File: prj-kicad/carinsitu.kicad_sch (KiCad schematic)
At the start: 57 parts, among them P1 BAT, P2 MOT, P3 CONN_3, P4 CONN_1, P5 CONN_4, SW1 SWITCH_SLIDE, U1 ESP8285, U2 MIC2860, U3 MAX17205, U4 SN74LVC1T45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

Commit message: Fix schematic DRC
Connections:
- no-connect marks 7 -> 15
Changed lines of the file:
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@@
   (junction (at 40.64 181.61) (diameter 0) (color 0 0 0 0)
   )
+  (junction (at 71.12 128.27) (diameter 0) (color 0 0 0 0)
+  )
   (junction (at 50.8 73.66) (diameter 0) (color 0 0 0 0)
   )
@@
   )
   (no_connect (at 210.82 96.52))
+  (no_connect (at 78.74 40.64))
+  (no_connect (at 78.74 35.56))
   (no_connect (at 210.82 101.6))
+  (no_connect (at 82.55 175.26))
   (no_connect (at 125.73 31.75))
+  (no_connect (at 78.74 43.18))
   (no_connect (at 111.76 48.26))
+  (no_connect (at 78.74 38.1))
   (no_connect (at 82.55 165.1))
+  (no_connect (at 78.74 45.72))
+  (no_connect (at 111.76 45.72))
   (no_connect (at 259.08 109.22))
   (no_connect (at 66.04 133.35))
+  (no_connect (at 78.74 48.26))
   (wire (pts (xy 242.57 148.59) (xy 242.57 137.16))
     (stroke (width 0) (type default) (color 0 0 0 0))
@@
     (stroke (width 0) (type default) (color 0 0 0 0))
   )
+  (wire (pts (xy 71.12 128.27) (xy 72.39 128.27))
+    (stroke (width 0) (type default) (color 0 0 0 0))
+  )
   (wire (pts (xy 128.27 78.74) (xy 128.27 77.47))
     (stroke (width 0) (type default) (color 0 0 0 0))
@@
     (pin "2")
   )
+  (symbol (lib_id "power:PWR_FLAG") (at 72.39 128.27 270) (unit 1)
+    (in_bom yes) (on_board yes) (fields_autoplaced)
+    (property "Reference" "#FLG0101" (id 0) (at 74.295 128.27 0)
+      (effects (font (size 1.27 1.27)) hide)
+    )
+    (property "Value" "PWR_FLAG" (id 1) (at 75.565 128.7038 90)
+      (effects (font (size 1.27 1.27)) (justify left))
+    )
+    (property "Footprint" "" (id 2) (at 72.39 128.27 0)
+      (effects (font (size 1.27 1.27)) hide)
+    )
+    (property "Datasheet" "~" (id 3) (at 72.39 128.27 0)
+      (effects (font (size 1.27 1.27)) hide)
+    )
+    (pin "1")
+  )
   (sheet (at 102.87 120.65) (size 67.31 41.91) (fields_autoplaced)
     (stroke (width 0) (type solid) (color 0 0 0 0))
@@
   )
   (symbol_instances
+    (path "/72432868-7bcd-4a68-adb7-1800ac178c45"
+      (reference "#FLG0101") (unit 1) (value "PWR_FLAG") (footprint "")
+    )
+    (path "/00000000-0000-0000-0000-00005d24ff79/10e431fa-02a9-4f70-8adb-f2c11e9e1180"
+      (reference "#FLG0102") (unit 1) (value "PWR_FLAG") (footprint "")
+    )
+    (path "/00000000-0000-0000-0000-00005d24ff79/f57f5fed-3b45-4cb3-9d9d-82cd0401c166"
+      (reference "#FLG0103") (unit 1) (value "PWR_FLAG") (footprint "")
+    )
     (path "/00000000-0000-0000-0000-00005d08ea24"
       (reference "#PWR01") (unit 1) (value "GND") (footprint "")

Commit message: Do TODO for rear lights
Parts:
- removed D3: LED_APA106, carinsitu:LED-APA106, symbol carinsitu:LED_APA106
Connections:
- net at D4.4 (DIN): now also U4.4 (B)
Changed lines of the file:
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@@
     (stroke (width 0) (type default) (color 0 0 0 0))
   )
+  (wire (pts (xy 254 99.06) (xy 254 106.68))
+    (stroke (width 0) (type default) (color 0 0 0 0))
+  )
   (wire (pts (xy 199.39 111.76) (xy 199.39 113.03))
     (stroke (width 0) (type default) (color 0 0 0 0))
@@
     (stroke (width 0) (type default) (color 0 0 0 0))
   )
-  (wire (pts (xy 250.19 87.63) (xy 250.19 99.06))
-    (stroke (width 0) (type default) (color 0 0 0 0))
-  )
   (wire (pts (xy 71.12 128.27) (xy 66.04 128.27))
     (stroke (width 0) (type default) (color 0 0 0 0))
@@
     (stroke (width 0) (type default) (color 0 0 0 0))
   )
-  (wire (pts (xy 250.19 87.63) (xy 259.08 87.63))
-    (stroke (width 0) (type default) (color 0 0 0 0))
-  )
   (wire (pts (xy 109.22 43.18) (xy 109.22 40.64))
     (stroke (width 0) (type default) (color 0 0 0 0))
@@
     (stroke (width 0) (type default) (color 0 0 0 0))
   )
-  (wire (pts (xy 256.54 92.71) (xy 259.08 92.71))
-    (stroke (width 0) (type default) (color 0 0 0 0))
-  )
   (wire (pts (xy 193.04 86.36) (xy 193.04 87.63))
     (stroke (width 0) (type default) (color 0 0 0 0))
@@
     (stroke (width 0) (type default) (color 0 0 0 0))
   )
-  (wire (pts (xy 250.19 99.06) (xy 246.38 99.06))
+  (wire (pts (xy 246.38 99.06) (xy 254 99.06))
     (stroke (width 0) (type default) (color 0 0 0 0))
   )
@@
     (stroke (width 0) (type default) (color 0 0 0 0))
   )
-  (wire (pts (xy 256.54 82.55) (xy 256.54 85.09))
-    (stroke (width 0) (type default) (color 0 0 0 0))
-  )
   (wire (pts (xy 227.33 137.16) (xy 228.6 137.16))
     (stroke (width 0) (type default) (color 0 0 0 0))
@@
     (stroke (width 0) (type default) (color 0 0 0 0))
   )
-  (wire (pts (xy 256.54 95.25) (xy 256.54 92.71))
-    (stroke (width 0) (type default) (color 0 0 0 0))
-  )
   (wire (pts (xy 196.85 110.49) (xy 196.85 111.76))
     (stroke (width 0) (type default) (color 0 0 0 0))
@@
     (stroke (width 0) (type default) (color 0 0 0 0))
   )
-  (wire (pts (xy 259.08 90.17) (xy 254 90.17))
-    (stroke (width 0) (type default) (color 0 0 0 0))
-  )
   (wire (pts (xy 242.57 137.16) (xy 246.38 137.16))
     (stroke (width 0) (type default) (color 0 0 0 0))
@@
     (stroke (width 0) (type default) (color 0 0 0 0))
   )
-  (wire (pts (xy 256.54 85.09) (xy 259.08 85.09))
-    (stroke (width 0) (type default) (color 0 0 0 0))
-  )
   (wire (pts (xy 43.18 50.8) (xy 45.72 50.8))
     (stroke (width 0) (type default) (color 0 0 0 0))
@@
     (stroke (width 0) (type default) (color 0 0 0 0))
   )
-  (wire (pts (xy 254 90.17) (xy 254 106.68))
-    (stroke (width 0) (type default) (color 0 0 0 0))
-  )
   (wire (pts (xy 43.18 44.45) (xy 45.72 44.45))
     (stroke (width 0) (type default) (color 0 0 0 0))
@@
     (pin "1")
   )
-  (symbol (lib_id "carinsitu:LED_APA106") (at 266.7 88.9 0) (unit 1)
-    (in_bom yes) (on_board yes)
-    (property "Reference" "D3" (id 0) (at 266.7 82.55 0)
-      (effects (font (size 1.524 1.524)))
-    )
-    (property "Value" "LED_APA106" (id 1) (at 266.7 88.9 90)
-      (effects (font (size 1.016 1.016)))
-    )
-    (property "Footprint" "carinsitu:LED-APA106" (id 2) (at 266.7 88.9 0)
-      (effects (font (size 1.524 1.524)) hide)
-    )
-    (property "Datasheet" "" (id 3) (at 266.7 88.9 0)
-      (effects (font (size 1.524 1.524)))
-    )
-    (pin "1")
-    (pin "2")
-    (pin "3")
-    (pin "4")
-  )
   (symbol (lib_id "carinsitu:LED_APA106") (at 266.7 107.95 0) (unit 1)
     (in_bom yes) (on_board yes)
@@
     (pin "4")
   )
-  (symbol (lib_id "carinsitu:+5V") (at 256.54 82.55 0) (unit 1)
-    (in_bom yes) (on_board yes)
-    (property "Reference" "#PWR027" (id 0) (at 256.54 83.566 0)
-      (effects (font (size 0.762 0.762)) hide)
-    )
-    (property "Value" "+5V" (id 1) (at 256.54 79.756 0)
-      (effects (font (size 0.762 0.762)))
-    )
-    (property "Footprint" "" (id 2) (at 256.54 82.55 0)
-      (effects (font (size 1.524 1.524)))
-    )
-    (property "Datasheet" "" (id 3) (at 256.54 82.55 0)
-      (effects (font (size 1.524 1.524)))
-    )
-    (pin "1")
-  )
-  (symbol (lib_id "carinsitu:GND") (at 256.54 95.25 0) (unit 1)
-    (in_bom yes) (on_board yes)
-    (property "Reference" "#PWR028" (id 0) (at 256.54 95.25 0)
-      (effects (font (size 0.762 0.762)) hide)
-    )
-    (property "Value" "GND" (id 1) (at 256.54 97.028 0)
-      (effects (font (size 0.762 0.762)) hide)
-    )
-    (property "Footprint" "" (id 2) (at 256.54 95.25 0)
-      (effects (font (size 1.524 1.524)))
-    )
-    (property "Datasheet" "" (id 3) (at 256.54 95.25 0)
-      (effects (font (size 1.524 1.524)))
-    )
-    (pin "1")
-  )
   (symbol (lib_id "carinsitu:+5V") (at 256.54 101.6 0) (unit 1)
     (in_bom yes) (on_board yes)
@@
       (reference "#PWR026") (unit 1) (value "GND") (footprint "")
     )
-    (path "/00000000-0000-0000-0000-00005d24affe"
-      (reference "#PWR027") (unit 1) (value "+5V") (footprint "")
-    )
-    (path "/00000000-0000-0000-0000-00005d24b1a0"
-      (reference "#PWR028") (unit 1) (value "GND") (footprint "")
-    )
     (path "/00000000-0000-0000-0000-00005d24b240"
       (reference "#PWR029") (unit 1) (value "+5V") (footprint "")
@@
       (reference "D2") (unit 1) (value "LED") (footprint "carinsitu:LED")
     )
-    (path "/00000000-0000-0000-0000-00005d24ad1c"
-      (reference "D3") (unit 1) (value "LED_APA106") (footprint "carinsitu:LED-APA106")
-    )
     (path "/00000000-0000-0000-0000-00005d24ade3"

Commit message: Do the remaining TODO list
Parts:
- removed P4: CONN_1, carinsitu:TP, symbol carinsitu:CONN_1
- added P4: CONN_3, carinsitu:CONN_61300311021, symbol carinsitu:CONN_3
- added SW2: SW_Push, Button_Switch_SMD:SW_Push_1P1T_NO_6x6mm_H9.5mm, symbol Switch:SW_Push
- added TP10, TP11: CONN_1, carinsitu:TP, symbol carinsitu:CONN_1
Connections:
- net +3V3: now also TP11.1
- net +5V: now also P4.1 (P1), TP10.1
- net GND: now also P4.3 (P3), SW2.1
- net VTX: now also P4.2 (P2)
- net at C2.1, U1.32 (RST), U1.8 (XPD): now also SW2.2

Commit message: PCB: Various adjustments
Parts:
- P4: footprint carinsitu:CONN_61300311021 -> carinsitu:CONN_61300311121
- SW2: value SW_Push -> Reset
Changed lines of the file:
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@@
       (effects (font (size 1.27 1.27)) (justify right))
     )
-    (property "Value" "SW_Push" (id 1) (at 96.52 44.45 0)
+    (property "Value" "Reset" (id 1) (at 97.155 45.72 0)
       (effects (font (size 1.27 1.27)) (justify right))
     )
@@
       (effects (font (size 1.016 1.016)) (justify right))
     )
-    (property "Footprint" "carinsitu:CONN_61300311021" (id 2) (at 266.7 19.05 0)
+    (property "Footprint" "carinsitu:CONN_61300311121" (id 2) (at 266.7 19.05 0)
       (effects (font (size 1.524 1.524)) hide)
     )
@@
     )
     (path "/d8eed33f-3afa-4021-9e01-1f7eb77f574b"
-      (reference "P4") (unit 1) (value "CONN_3") (footprint "carinsitu:CONN_61300311021")
+      (reference "P4") (unit 1) (value "CONN_3") (footprint "carinsitu:CONN_61300311121")
     )
     (path "/00000000-0000-0000-0000-00005d2e467b"
@@
     )
     (path "/c0953f61-06fb-48b6-8efa-bb086c1a612b"
-      (reference "SW2") (unit 1) (value "SW_Push") (footprint "Button_Switch_SMD:SW_Push_1P1T_NO_6x6mm_H9.5mm")
+      (reference "SW2") (unit 1) (value "Reset") (footprint "Button_Switch_SMD:SW_Push_1P1T_NO_6x6mm_H9.5mm")
     )
     (path "/00000000-0000-0000-0000-00005d24ff79/00000000-0000-0000-0000-00005d25331a"

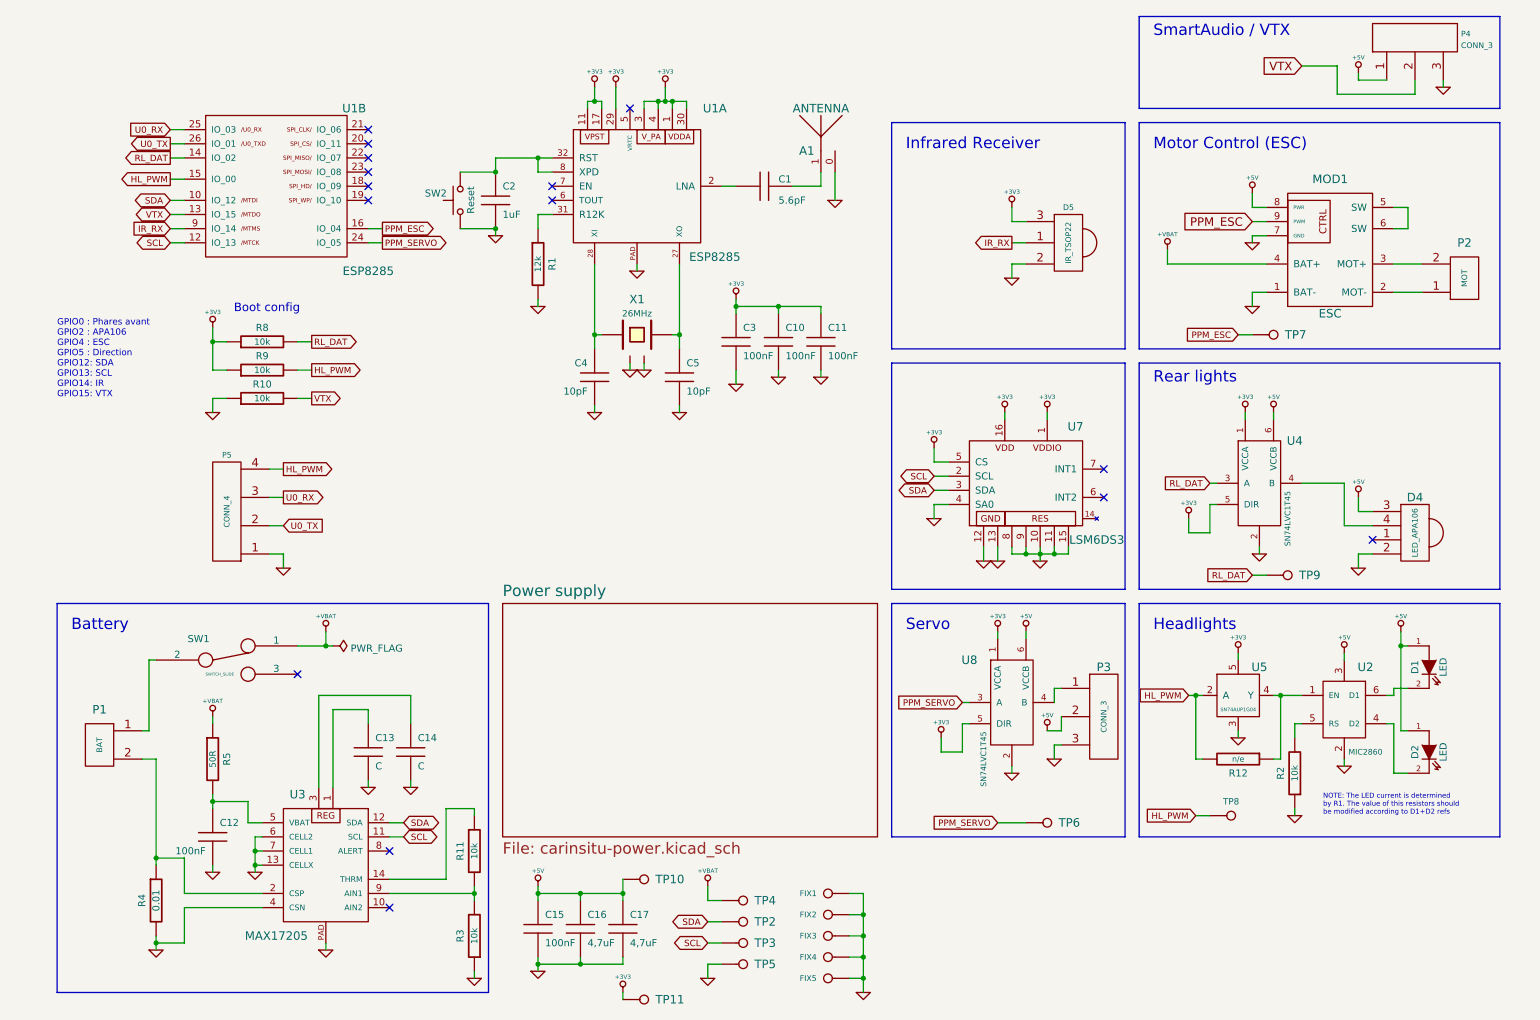
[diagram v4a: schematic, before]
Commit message: Change MCU and VTX + related (see detailed message)
The VTX module is changed and now communicates with an UART.
The MCU and its powering are replaced by a LoLin D1 mini pro module.
IO are remapped
Removed inverter on headlights (not needed with new mapping)
Added pull-up on I²C and pull-down on ESC and Headlights
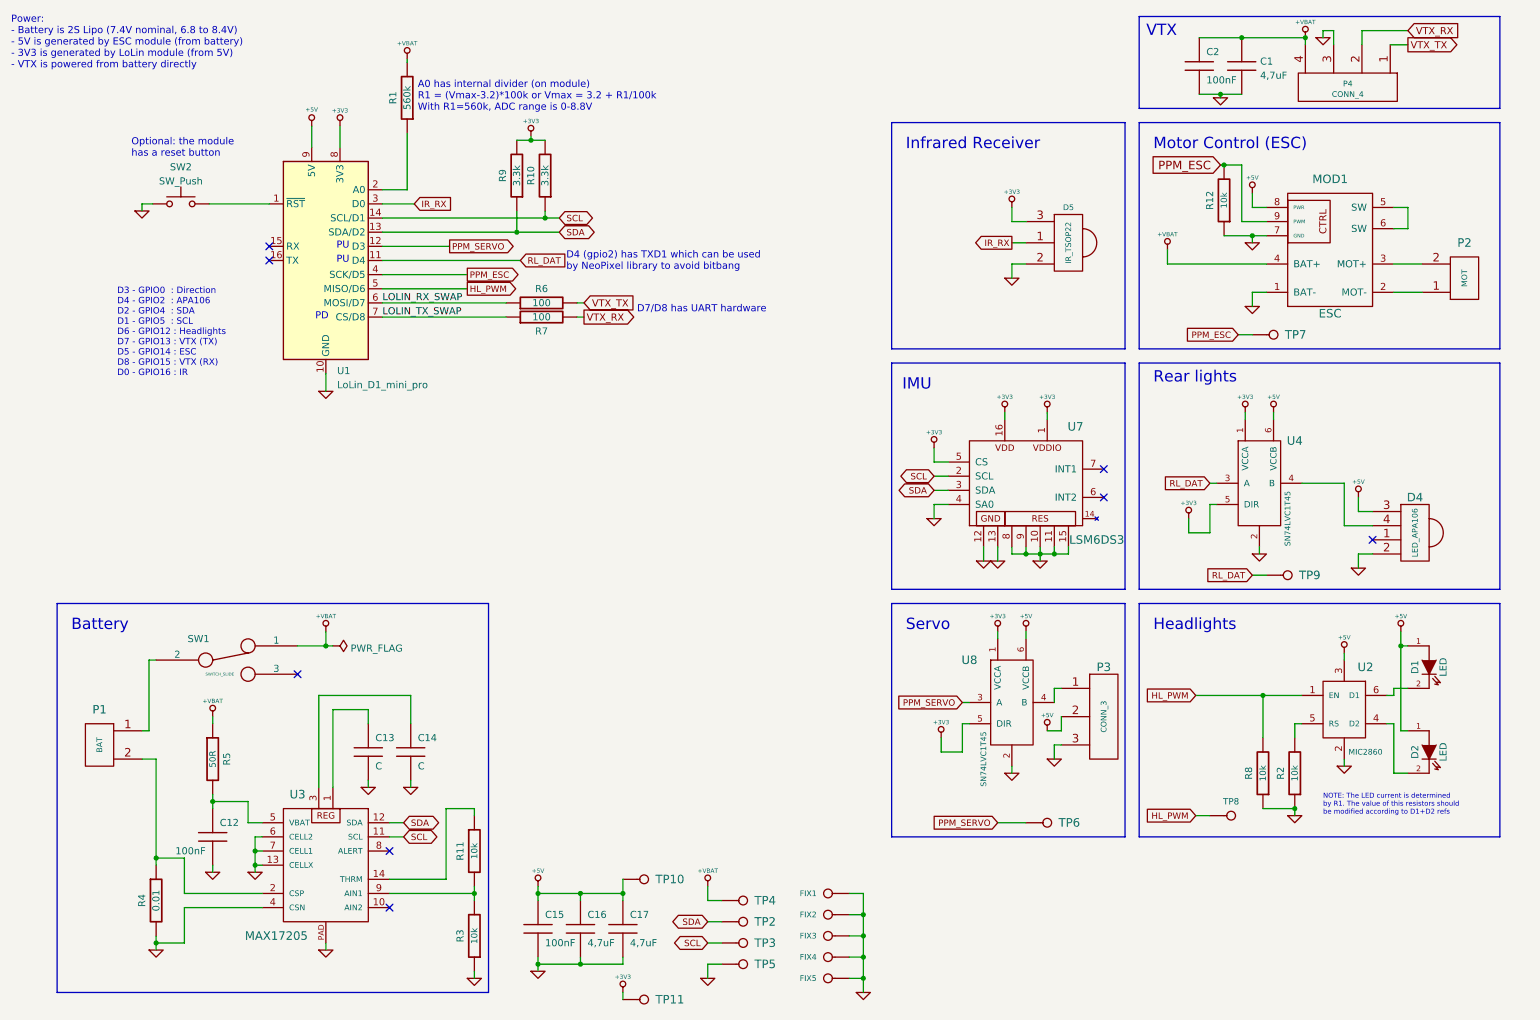
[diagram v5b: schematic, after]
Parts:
- removed A1: ANTENNA, carinsitu:CONN_UFL-R-SMT-1, symbol carinsitu:ANTENNA
- removed C10, C11, C3: 100nF, carinsitu:SMD0603, symbol carinsitu:C
- removed C4, C5: 10pF, carinsitu:SMD0603, symbol carinsitu:C
- removed P4: CONN_3, carinsitu:CONN_61300311121, symbol carinsitu:CONN_3
- removed P5: CONN_4, carinsitu:CONN_61300411121, symbol carinsitu:CONN_4
- removed U1: ESP8285, carinsitu:QFN32, symbol carinsitu:ESP8285
- removed U5: SN74AUP1G04, carinsitu:SC70-5, symbol carinsitu:SN74AUP1G04
- removed X1: 26MHz, carinsitu:Q_3.2x2.5, symbol carinsitu:CRYSTAL4
- added P4: CONN_4, symbol carinsitu:CONN_4
- added R6, R7: 100, symbol carinsitu:R
- added U1: LoLin_D1_mini_pro, Module:WEMOS_D1_mini_light, symbol MCU_Module:WeMos_D1_mini
- C1: value 5.6pF -> 4,7uF; footprint carinsitu:SMD0603 -> (none)
- C2: value 1uF -> 100nF
- R1: value 12k -> 560k; footprint carinsitu:SMD0603 -> (none)
- R10, R9: value 10k -> 3.3k; footprint carinsitu:SMD0603 -> (none)
- R12: value n/e -> 10k; footprint carinsitu:SMD0603 -> carinsitu:SMD0805
- R8: footprint carinsitu:SMD0603 -> carinsitu:SMD0805
- SW2: value Reset -> SW_Push; footprint Button_Switch_SMD:SW_Push_1P1T_NO_6x6mm_H9.5mm -> (none)
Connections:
- net VTX is gone; now on net +3V3: R10.2
- net +3V3: now also R9.2, U1.8 (3V3); no longer R8.1, R9.1
- net +5V: now also U1.9 (5V)
- net +VBAT: now also C1.1, C2.1, R1.2, P4.4
- net GND: now also C1.2, R12.1, R8.1, P4.3 (P3), U1.10 (GND); no longer R1.2, R10.1
- net HL_PWM: now also R8.2, U2.1 (EN), U1.5 (MISO/D6); no longer R12.2, R9.2
- net IR_RX: now also U1.3 (D0)
- net PPM_ESC: now also R12.2, U1.4 (SCK/D5)
- net PPM_SERVO: now also U1.12 (D3)
- net RL_DAT: now also U1.11 (D4); no longer R8.2
- net SCL: now also R10.1, U1.14 (SCL/D1)
- net SDA: now also R9.1, U1.13 (SDA/D2)
- net at SW2.2: now also U1.1 (~{RST}); no longer C2.1
- net at R1.1: now also U1.2 (A0)
- new net LOLIN_RX_SWAP: R6.1, U1.6 (MOSI/D7)
- new net LOLIN_TX_SWAP: R7.1, U1.7 (CS/D8)
- new net VTX_RX: P4.2 (P2), R7.2
- new net VTX_TX: P4.1 (P1), R6.2
- no-connect marks 15 -> 8
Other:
- removed sheet Power supply
- note added: "A0 has internal divider (on module) R1 = (Vmax-3.2)*100k or Vmax = 3.2 + R1/100k With R1=560k, ADC range is 0-8.8V"
- note added: "D3 - GPIO0 : Direction D4 - GPIO2 : APA106 D2 - GPIO4 : SDA D1 - GPIO5 : SCL D6 - GPIO12 : Headlights D7 - GPIO13 : VTX (TX) D5 - GPIO14 : ESC D8 - GPIO15 : VTX (RX) D0 - GPIO16 : IR"
- note added: "D4 (gpio2) has TXD1 which can be used by NeoPixel library to avoid bitbang"
- note added: "D7/D8 has UART hardware"
- note added: "IMU"
- note added: "Optional: the module has a reset button"
- note added: "PD"
- note added: "PU"
- note added: "Power: - Battery is 2S Lipo (7.4V nominal, 6.8 to 8.4V) - 5V is generated by ESC module (from battery) - 3V3 is generated by LoLin module (from 5V) - VTX is powered from battery directly"
- note added: "VTX"
- note removed: "Boot config"
- note removed: "GPIO0 : Phares avant GPIO2 : APA106 GPIO4 : ESC GPIO5 : Direction GPIO12: SDA GPIO13: SCL GPIO14: IR GPIO15: VTX"
- note removed: "SmartAudio / VTX"

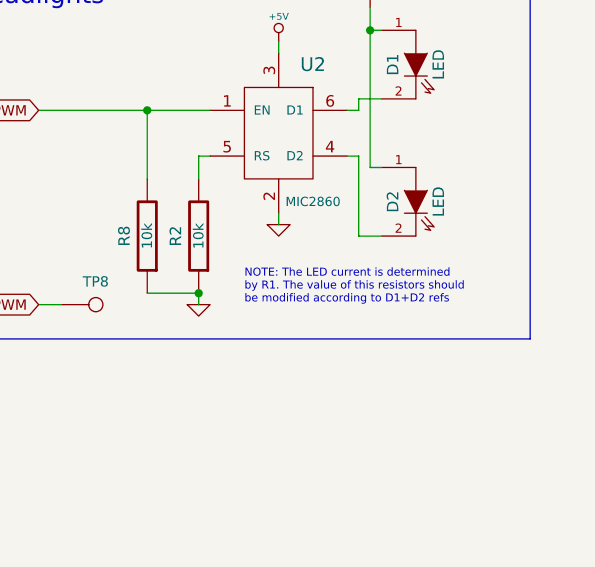
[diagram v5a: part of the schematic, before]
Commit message: Add precisions in note for headlights
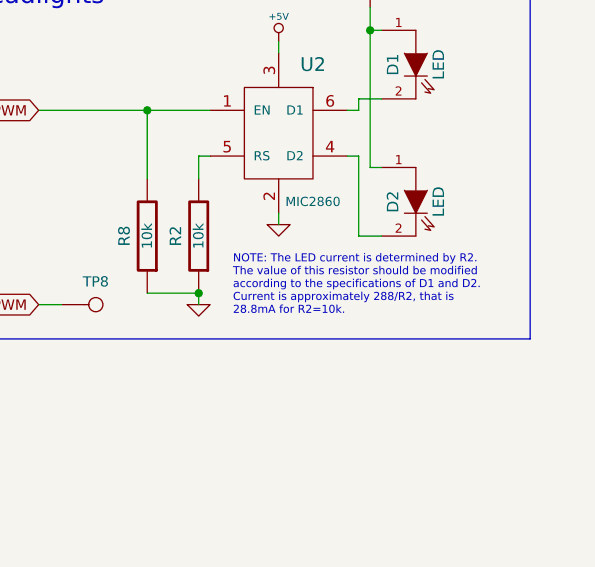
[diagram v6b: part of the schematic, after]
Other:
- note added: "NOTE: The LED current is determined by R2. The value of this resistor should be modified according to the specifications of D1 and D2. Current is approximately 288/R2, that is 28.8mA for R2=10k."
- note removed: "NOTE: The LED current is determined by R1. The value of this resistors should be modified according to D1+D2 refs"
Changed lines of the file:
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@@
     (effects (font (size 1.27 1.27)) (justify left bottom))
   )
-  (text "NOTE: The LED current is determined\nby R1. The value of this resistors should\nbe modified according to D1+D2 refs"
-    (at 250.19 158.75 0)
+  (text "NOTE: The LED current is determined by R2.\nThe value of this resistor should be modified\naccording to the specifications of D1 and D2.\nCurrent is approximately 288/R2, that is\n28.8mA for R2=10k."
+    (at 248.92 160.02 0)
     (effects (font (size 0.889 0.889)) (justify left bottom))
   )
